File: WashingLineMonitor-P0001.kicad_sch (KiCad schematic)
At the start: 0 parts

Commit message: Added QI wireless charging circuit
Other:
- added sheet Input Power (INPUT_POWER.kicad_sch)
- added sheet MCU (MCU.kicad_sch)
- added sheet Moisture Sensor (Moisture_sensor.kicad_sch)
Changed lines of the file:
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@@
 	(generator_version "9.0")
 	(paper "A4")
+	(sheet
+		(at 44.45 25.4)
+		(size 20.32 19.05)
+		(exclude_from_sim no)
+		(in_bom yes)
+		(on_board yes)
+		(dnp no)
+		(fields_autoplaced yes)
+		(stroke
+			(width 0.1524)
+			(type solid)
+		)
+		(fill
+			(color 0 0 0 0.0000)
+		)
+		(property "Sheetname" "Moisture Sensor"
+			(at 44.45 24.6884 0)
+			(effects
+				(font
+					(size 1.27 1.27)
+				)
+				(justify left bottom)
+			)
+		)
+		(property "Sheetfile" "Moisture_sensor.kicad_sch"
+			(at 44.45 45.0346 0)
+			(effects
+				(font
+					(size 1.27 1.27)
+				)
+				(justify left top)
+			)
+		)
+		(instances
+			(project "WashingLineMonitor-P0001"
+				(path "/09468f75-1295-4aed-9d66-1cbb46f6d9f7"
+					(page "2")
+				)
+			)
+		)
+	)
+	(sheet
+		(at 81.28 25.4)
+		(size 20.32 19.05)
+		(exclude_from_sim no)
+		(in_bom yes)
+		(on_board yes)
+		(dnp no)
+		(fields_autoplaced yes)
+		(stroke
+			(width 0.1524)
+			(type solid)
+		)
+		(fill
+			(color 0 0 0 0.0000)
+		)
+		(property "Sheetname" "MCU"
+			(at 81.28 24.6884 0)
+			(effects
+				(font
+					(size 1.27 1.27)
+				)
+				(justify left bottom)
+			)
+		)
+		(property "Sheetfile" "MCU.kicad_sch"
+			(at 81.28 45.0346 0)
+			(effects
+				(font
+					(size 1.27 1.27)
+				)
+				(justify left top)
+			)
+		)
+		(instances
+			(project "WashingLineMonitor-P0001"
+				(path "/09468f75-1295-4aed-9d66-1cbb46f6d9f7"
+					(page "3")
+				)
+			)
+		)
+	)
+	(sheet
+		(at 110.49 25.4)
+		(size 20.32 19.05)
+		(exclude_from_sim no)
+		(in_bom yes)
+		(on_board yes)
+		(dnp no)
+		(fields_autoplaced yes)
+		(stroke
+			(width 0.1524)
+			(type solid)
+		)
+		(fill
+			(color 0 0 0 0.0000)
+		)
+		(property "Sheetname" "Input Power"
+			(at 110.49 24.6884 0)
+			(effects
+				(font
+					(size 1.27 1.27)
+				)
+				(justify left bottom)
+			)
+		)
+		(property "Sheetfile" "INPUT_POWER.kicad_sch"
+			(at 110.49 45.0346 0)
+			(effects
+				(font
+					(size 1.27 1.27)
+				)
+				(justify left top)
+			)
+		)
+		(instances
+			(project "WashingLineMonitor-P0001"
+				(path "/09468f75-1295-4aed-9d66-1cbb46f6d9f7"
+					(page "4")
+				)
+			)
+		)
+	)
 	(sheet_instances
 		(path "/"

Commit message: Completed first iteration and reviews
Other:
- company: (none) -> Horatio Pistachio
- title: (none) -> WashingLineMonitor-P0001
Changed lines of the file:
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@@
 	(generator_version "9.0")
 	(paper "A4")
+	(title_block
+		(title "WashingLineMonitor-P0001")
+		(date "2025-09-14")
+		(rev "AB")
+		(company "Horatio Pistachio")
+		(comment 1 "AA - Original")
+		(comment 2 "AB - Updated from AI review")
+	)
 	(sheet
 		(at 44.45 25.4)

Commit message: commit of local files before designing next version
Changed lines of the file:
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@@
 		(comment 2 "AB - Updated from AI review")
+	)
+	(text_box "Changes\n-[ ] add power switch(manual plus an sense of if the cloth is connected)\n-[ ] think through wiring better (add mini jst connectors for batt and sense)\n-[ ] add label to battery terminals\n-[ ] use standard 2.54mm sized holes\n-[ ] Removed or up voltage on ESD diode on sensor input. the 3v3 casues issues\n-[ ] Buy several different sensor resistors or reduce (500k is likely too high)\n-[ ] Improve ESD protection\n-[ ] add flex in the line mounting clips to suit metal washing racks"
+		(exclude_from_sim no)
+		(at 50.8 74.93 0)
+		(size 97.79 55.88)
+		(margins 0.9525 0.9525 0.9525 0.9525)
+		(stroke
+			(width 0)
+			(type solid)
+		)
+		(fill
+			(type none)
+		)
+		(effects
+			(font
+				(size 1.27 1.27)
+			)
+			(justify left top)
+		)
 	)
 	(sheet

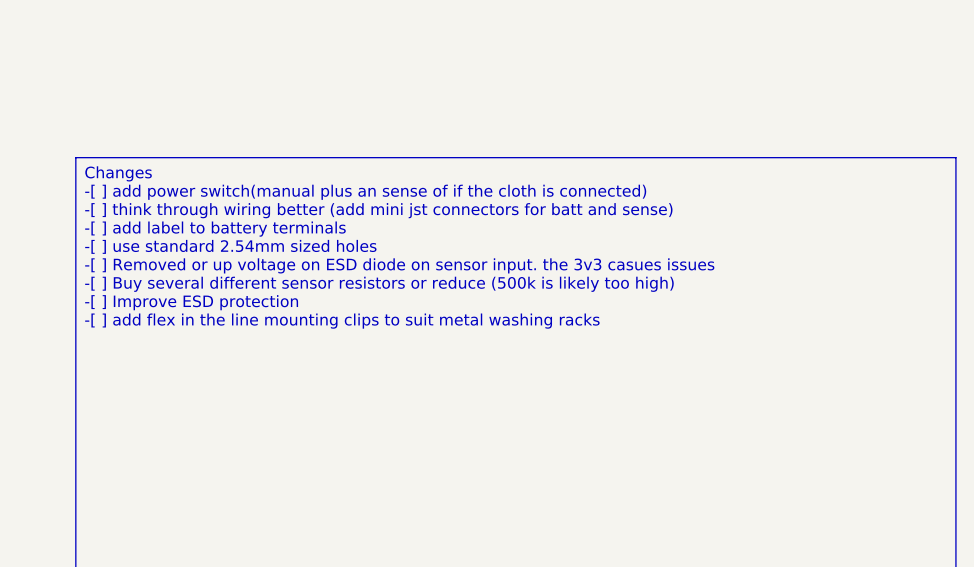
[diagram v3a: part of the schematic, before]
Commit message: updated schematic from review
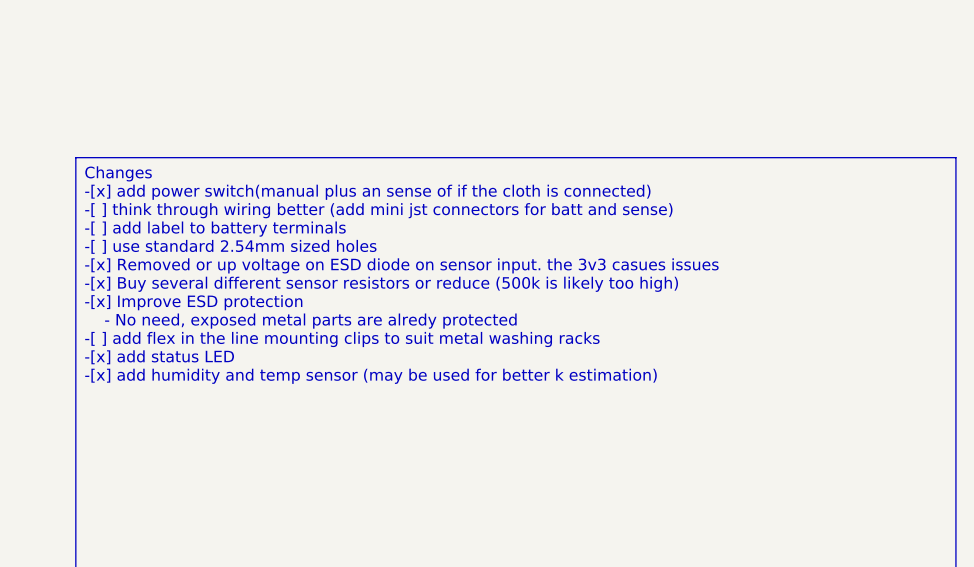
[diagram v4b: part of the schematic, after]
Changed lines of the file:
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@@
 (kicad_sch
-	(version 20250114)
+	(version 20260306)
 	(generator "eeschema")
-	(generator_version "9.0")
+	(generator_version "10.0")
 	(paper "A4")
 	(title_block
@@
 		(comment 2 "AB - Updated from AI review")
 	)
-	(text_box "Changes\n-[ ] add power switch(manual plus an sense of if the cloth is connected)\n-[ ] think through wiring better (add mini jst connectors for batt and sense)\n-[ ] add label to battery terminals\n-[ ] use standard 2.54mm sized holes\n-[ ] Removed or up voltage on ESD diode on sensor input. the 3v3 casues issues\n-[ ] Buy several different sensor resistors or reduce (500k is likely too high)\n-[ ] Improve ESD protection\n-[ ] add flex in the line mounting clips to suit metal washing racks"
+	(text_box "Changes\n-[x] add power switch(manual plus an sense of if the cloth is connected)\n-[ ] think through wiring better (add mini jst connectors for batt and sense)\n-[ ] add label to battery terminals\n-[ ] use standard 2.54mm sized holes\n-[x] Removed or up voltage on ESD diode on sensor input. the 3v3 casues issues\n-[x] Buy several different sensor resistors or reduce (500k is likely too high)\n-[x] Improve ESD protection\n	- No need, exposed metal parts are alredy protected\n-[ ] add flex in the line mounting clips to suit metal washing racks\n-[x] add status LED\n-[x] add humidity and temp sensor (may be used for better k estimation)"
 		(exclude_from_sim no)
 		(at 50.8 74.93 0)
@@
 		)
 		(fill
-			(color 0 0 0 0.0000)
+			(color 0 0 0 0)
 		)
 		(property "Sheetname" "Moisture Sensor"
 			(at 44.45 24.6884 0)
+			(show_name no)
+			(do_not_autoplace no)
 			(effects
 				(font
@@
 		(property "Sheetfile" "Moisture_sensor.kicad_sch"
 			(at 44.45 45.0346 0)
+			(show_name no)
+			(do_not_autoplace no)
 			(effects
 				(font
@@
 		)
 		(fill
-			(color 0 0 0 0.0000)
+			(color 0 0 0 0)
 		)
 		(property "Sheetname" "MCU"
 			(at 81.28 24.6884 0)
+			(show_name no)
+			(do_not_autoplace no)
 			(effects
 				(font
@@
 		(property "Sheetfile" "MCU.kicad_sch"
 			(at 81.28 45.0346 0)
+			(show_name no)
+			(do_not_autoplace no)
 			(effects
 				(font
@@
 		)
 		(fill
-			(color 0 0 0 0.0000)
+			(color 0 0 0 0)
 		)
 		(property "Sheetname" "Input Power"
 			(at 110.49 24.6884 0)
+			(show_name no)
+			(do_not_autoplace no)
 			(effects
 				(font
@@
 		(property "Sheetfile" "INPUT_POWER.kicad_sch"
 			(at 110.49 45.0346 0)
+			(show_name no)
+			(do_not_autoplace no)
 			(effects
 				(font

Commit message: Minor pre release changes
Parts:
- added FID1, FID2, FID3: Fiducial, Fiducial:Fiducial_0.5mm_Mask1mm, symbol Mechanical:Fiducial
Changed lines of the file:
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@@
 	(title_block
 		(title "WashingLineMonitor-P0001")
-		(date "2025-09-14")
-		(rev "AB")
+		(date "2026-06-06")
+		(rev "AC")
 		(company "Horatio Pistachio")
 		(comment 1 "AA - Original")
 		(comment 2 "AB - Updated from AI review")
-	)
-	(text_box "Changes\n-[x] add power switch(manual plus an sense of if the cloth is connected)\n-[ ] think through wiring better (add mini jst connectors for batt and sense)\n-[ ] add label to battery terminals\n-[ ] use standard 2.54mm sized holes\n-[x] Removed or up voltage on ESD diode on sensor input. the 3v3 casues issues\n-[x] Buy several different sensor resistors or reduce (500k is likely too high)\n-[x] Improve ESD protection\n	- No need, exposed metal parts are alredy protected\n-[ ] add flex in the line mounting clips to suit metal washing racks\n-[x] add status LED\n-[x] add humidity and temp sensor (may be used for better k estimation)"
+		(comment 3 "AC - Added Connector, Switch to ESP32 C3, added humidity sensor and power switch")
+	)
+	(symbol
+		(lib_id "Mechanical:Fiducial")
+		(at 34.29 191.77 0)
+		(unit 1)
+		(body_style 1)
 		(exclude_from_sim no)
-		(at 50.8 74.93 0)
-		(size 97.79 55.88)
-		(margins 0.9525 0.9525 0.9525 0.9525)
-		(stroke
-			(width 0)
-			(type solid)
-		)
-		(fill
-			(type none)
-		)
-		(effects
-			(font
-				(size 1.27 1.27)
-			)
-			(justify left top)
-		)
-	)
+		(in_bom no)
+		(on_board yes)
+		(in_pos_files yes)
+		(dnp no)
+		(fields_autoplaced yes)
+		(property "Reference" "FID2"
+			(at 36.83 190.4999 0)
+			(show_name no)
+			(do_not_autoplace no)
+			(effects
+				(font
+					(size 1.27 1.27)
+				)
+				(justify left)
+			)
+		)
+		(property "Value" "Fiducial"
+			(at 36.83 193.0399 0)
+			(show_name no)
+			(do_not_autoplace no)
+			(effects
+				(font
+					(size 1.27 1.27)
+				)
+				(justify left)
+			)
+		)
+		(property "Footprint" "Fiducial:Fiducial_0.5mm_Mask1mm"
+			(at 34.29 191.77 0)
+			(hide yes)
+			(show_name no)
+			(do_not_autoplace no)
+			(effects
+				(font
+					(size 1.27 1.27)
+				)
+			)
+		)
+		(property "Datasheet" ""
+			(at 34.29 191.77 0)
+			(hide yes)
+			(show_name no)
+			(do_not_autoplace no)
+			(effects
+				(font
+					(size 1.27 1.27)
+				)
+			)
+		)
+		(property "Description" "Fiducial Marker"
+			(at 34.29 191.77 0)
+			(hide yes)
+			(show_name no)
+			(do_not_autoplace no)
+			(effects
+				(font
+					(size 1.27 1.27)
+				)
+			)
+		)
+		(instances
+			(project "WashingLineMonitor-P0001"
+				(path "/09468f75-1295-4aed-9d66-1cbb46f6d9f7"
+					(reference "FID2")
+					(unit 1)
+				)
+			)
+		)
+	)
+	(symbol
+		(lib_id "Mechanical:Fiducial")
+		(at 48.26 191.77 0)
+		(unit 1)
+		(body_style 1)
+		(exclude_from_sim no)
+		(in_bom no)
+		(on_board yes)
+		(in_pos_files yes)
+		(dnp no)
+		(fields_autoplaced yes)
+		(property "Reference" "FID3"
+			(at 50.8 190.4999 0)
+			(show_name no)
+			(do_not_autoplace no)
+			(effects
+				(font
+					(size 1.27 1.27)
+				)
+				(justify left)
+			)
+		)
+		(property "Value" "Fiducial"
+			(at 50.8 193.0399 0)
+			(show_name no)
+			(do_not_autoplace no)
+			(effects
+				(font
+					(size 1.27 1.27)
+				)
+				(justify left)
+			)
+		)
+		(property "Footprint" "Fiducial:Fiducial_0.5mm_Mask1mm"
+			(at 48.26 191.77 0)
+			(hide yes)
+			(show_name no)
+			(do_not_autoplace no)
+			(effects
+				(font
+					(size 1.27 1.27)
+				)
+			)
+		)
+		(property "Datasheet" ""
+			(at 48.26 191.77 0)
+			(hide yes)
+			(show_name no)
+			(do_not_autoplace no)
+			(effects
+				(font
+					(size 1.27 1.27)
+				)
+			)
+		)
+		(property "Description" "Fiducial Marker"
+			(at 48.26 191.77 0)
+			(hide yes)
+			(show_name no)
+			(do_not_autoplace no)
+			(effects
+				(font
+					(size 1.27 1.27)
+				)
+			)
+		)
+		(instances
+			(project "WashingLineMonitor-P0001"
+				(path "/09468f75-1295-4aed-9d66-1cbb46f6d9f7"
+					(reference "FID3")
+					(unit 1)
+				)
+			)
+		)
+	)
+	(symbol
+		(lib_id "Mechanical:Fiducial")
+		(at 20.32 191.77 0)
+		(unit 1)
+		(body_style 1)
+		(exclude_from_sim no)
+		(in_bom no)
+		(on_board yes)
+		(in_pos_files yes)
+		(dnp no)
+		(fields_autoplaced yes)
+		(property "Reference" "FID1"
+			(at 22.86 190.4999 0)
+			(show_name no)
+			(do_not_autoplace no)
+			(effects
+				(font
+					(size 1.27 1.27)
+				)
+				(justify left)
+			)
+		)
+		(property "Value" "Fiducial"
+			(at 22.86 193.0399 0)
+			(show_name no)
+			(do_not_autoplace no)
+			(effects
+				(font
+					(size 1.27 1.27)
+				)
+				(justify left)
+			)
+		)
+		(property "Footprint" "Fiducial:Fiducial_0.5mm_Mask1mm"
+			(at 20.32 191.77 0)
+			(hide yes)
+			(show_name no)
+			(do_not_autoplace no)
+			(effects
+				(font
+					(size 1.27 1.27)
+				)
+			)
+		)
+		(property "Datasheet" ""
+			(at 20.32 191.77 0)
+			(hide yes)
+			(show_name no)
+			(do_not_autoplace no)
+			(effects
+				(font
+					(size 1.27 1.27)
+				)
+			)
+		)
+		(property "Description" "Fiducial Marker"
+			(at 20.32 191.77 0)
+			(hide yes)
+			(show_name no)
+			(do_not_autoplace no)
+			(effects
+				(font
+					(size 1.27 1.27)
+				)
+			)
+		)
+		(instances
+			(project "WashingLineMonitor-P0001"
+				(path "/09468f75-1295-4aed-9d66-1cbb46f6d9f7"
+					(reference "FID1")
+					(unit 1)
+				)
+			)
+		)
+	)
